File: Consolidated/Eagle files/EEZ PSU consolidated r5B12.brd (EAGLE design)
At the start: 337 x 150 mm, 555 parts, among them IC1 LTC3864EMSE#PBF, IC10 DAC8552IDGKTG4, IC11 ADG465SOT-23, IC12 TS5A9411DCKT, IC13 ADS1120IPWR, IC14 LP339D, IC15 TPD4E002DRLR, IC16 TPD2E001DZDR, IC17 ADUM3160BRWZ, IC18 TLC5925IDBQR, IC19 Si8641EC-B-IS1, IC2 LP2951SO8, IC20 SI8651EC-B-IS1, IC21 SI8651EC-B-IS1, IC22 LD1117ADT33TR, IC23 Si8641EC-B-IS1, IC24 PCA21125T/Q900/1,1, IC25 AT25256B-SSHL-B, IC26 W5500, IC27 BC857BS, IC28 TLC555, IC29 SN74LVC08APWR, IC3 TL783CKTTR, IC30 SN74LV1T34DBVR, IC31 TPS3705-33D, IC32 SN74LVC2G02DCTR, IC33 74LVC1G125GW.125, IC34 TPA6205A1DGN, IC4 LTC3260EMSE#PBF, IC5 TL072D, IC6 TL072D, IC7 LTC2050HVCS8#PBF, IC8 MCP23S17-E/SS, IC9 REF5025AIDG4, J1 BS-244DSM-R, J2 1-726388-2, J3 BS-244DSM-G, J4 BS-244DSM-B, J5 BS-244DSM-R, J6 BS-244DSM-B, J7 693072010801, Q1 IRFR5305, Q10 MMBT5401, Q11 MMBT5551, Q12 MMBT5551, Q13 IRLL2705PBF, Q14 IRFR48ZPBF, Q15 IRLML2246TRPBF, Q16 2N7002, Q17 MMBT5551, Q18 MMBT5401, Q19 MMBT5551, Q2 MMBT5401, Q20 MMBT5551, Q21 BTA26-600, Q22 BTA26-600, Q23 IRLL2705PBF, Q24 2N7002, Q25 2N7002, Q26 IRLML2246TRPBF, Q27 IRLML2246TRPBF, Q28 IRLML2246TRPBF, Q29 IRLML2246TRPBF, Q3 2N7002, Q30 2N7002, Q31 IRLML2246TRPBF, Q32 2N7002, Q33 2N7002, Q4 IRFP250N, Q5 BC857C, Q6 BCP56-16.115, Q7 IRFR5305, Q8 BCP56-16.115, Q9 MMBT5401, SW1 A101SYCQ04, SW2 EC12E20-24P24C-SW, SW3 1301.9316, X10 826629-5, X11 2411-01, X12 MC000006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

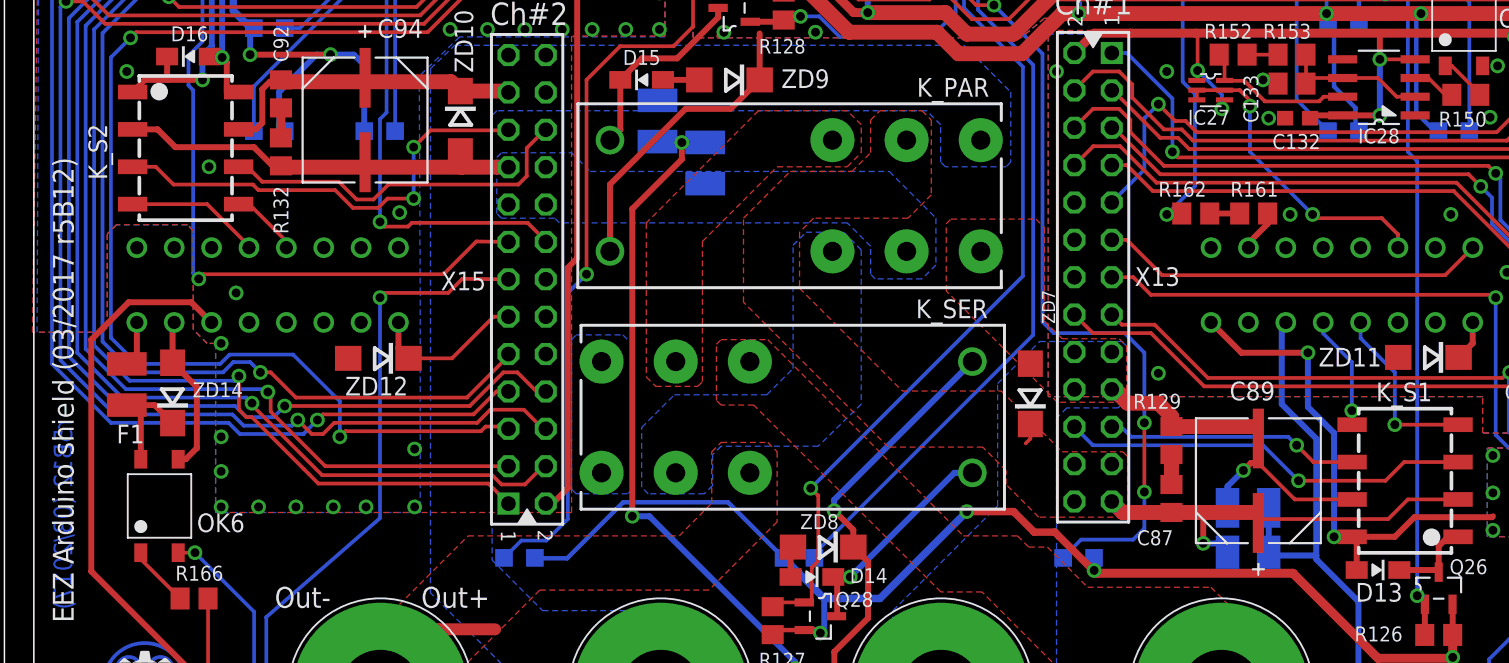
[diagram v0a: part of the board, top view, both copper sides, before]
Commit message: X14 pin 1, 2 swap, R177
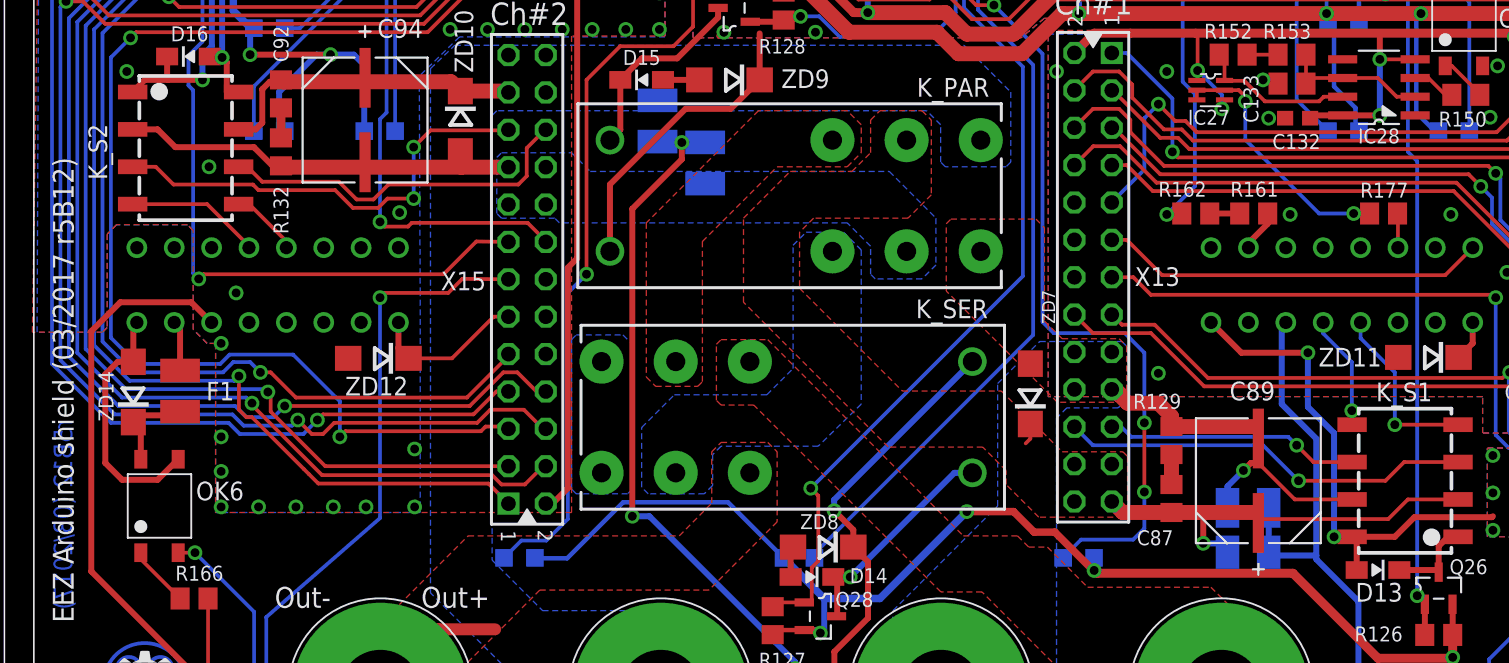
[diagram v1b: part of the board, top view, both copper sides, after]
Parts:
- added R177: 220R, rcl:R0805
- X1: value (none) -> 39-30-1039
- moved F1 3.65 mm to (118.9, 29.3)
- moved ZD14 2.67 mm to (115.8, 29.3)
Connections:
- removed net N$189: F1.2, X14.1, X14.1.1
- new net N$46: F1.2, X14.2, X14.2.1
- new net N$59: IC27.2, IC27.3, IC27.5, R177.2
- net N$188: now also X14.1, X14.1.1; no longer X14.2, X14.2.1
- net NTC_IN: now also R177.1; no longer IC27.2, IC27.3, IC27.5
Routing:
- net NTC_IN: track 21.3 -> 2.51 mm, vias 2 -> 0
- net N$59: track 0.00 -> 17.6 mm, vias 0 -> 2
- net N$188: track 10.9 -> 17.1 mm
- net N$46: track 0.00 -> 3.43 mm
- net N$189: track 3.10 -> 0.00 mm
- net N$187: track 7.43 -> 6.31 mm
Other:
- board text added: "R177"

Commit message: Encoder 25mm, new enclosure panels
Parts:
- SW2: value EC12E20-24P24C-SW -> PEC12R-4225F-S0024
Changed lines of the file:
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@@
 <attribute name="VALUE" x="102.0445" y="119.6975" size="1.27" layer="27" ratio="10"/>
 </element>
-<element name="SW2" library="EEZ_Lib1" package="EC12E_SW" value="EC12E20-24P24C-SW" x="216" y="62" smashed="yes" rot="MR270">
+<element name="SW2" library="EEZ_Lib1" package="EC12E_SW" value="PEC12R-4225F-S0024" x="216" y="62" smashed="yes" rot="MR270">
 <attribute name="NAME" x="209.185" y="69.7685" size="1.27" layer="26" rot="MR180"/>
 <attribute name="VALUE" x="206.455" y="62.5915" size="1.27" layer="28" rot="MR180"/>
@@
 </signal>
 </signals>
-<errors>
-</errors>
 </board>
 </drawing>

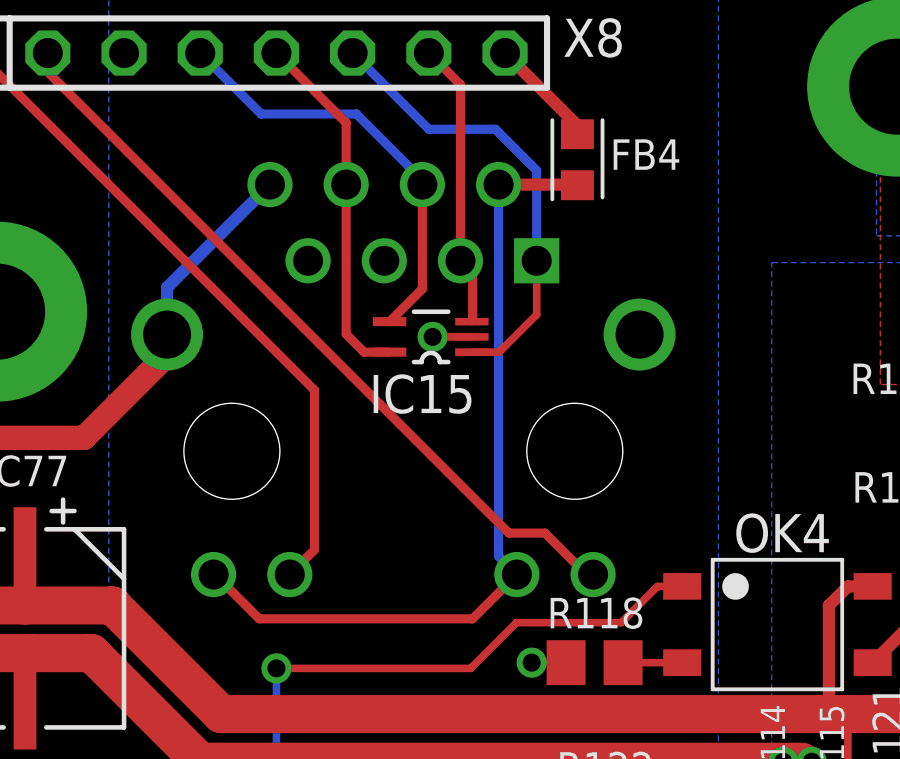
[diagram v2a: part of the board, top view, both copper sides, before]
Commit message: IC15 package, wire harness update
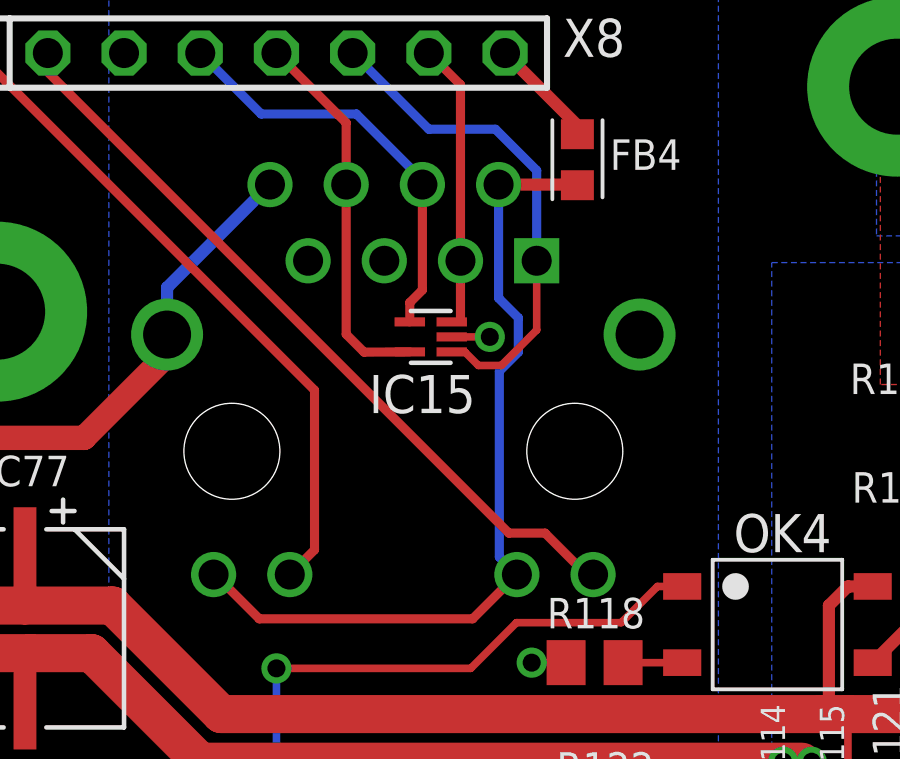
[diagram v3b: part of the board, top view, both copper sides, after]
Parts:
- IC15: value TPD4E002DRLR -> TPD4E002DRL; device EEZ_Lib1:SOT50P280X60-5N -> EEZ_Lib1:DRL5
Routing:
- net AUX_ETH_OUT+: track 15.2 -> 16.6 mm
- net AUX_ETH_IN-: track 12.0 -> 12.7 mm
- net N$24: track 27.2 -> 27.8 mm
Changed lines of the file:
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@@
 <layer number="17" name="Pads" color="6" fill="1" visible="yes" active="yes"/>
 <layer number="18" name="Vias" color="6" fill="1" visible="yes" active="yes"/>
-<layer number="19" name="Unrouted" color="14" fill="1" visible="no" active="yes"/>
+<layer number="19" name="Unrouted" color="14" fill="1" visible="yes" active="yes"/>
 <layer number="20" name="Dimension" color="15" fill="1" visible="yes" active="yes"/>
 <layer number="21" name="tPlace" color="7" fill="1" visible="yes" active="yes"/>
@@
 <attribute name="VALUE" x="91.948" y="47.8663" size="1.27" layer="27" ratio="10" rot="SR0"/>
 </element>
-<element name="IC15" library="EEZ_Lib1" package="SOT50P280X60-5N" value="TPD4E002DRLR" x="72.4535" y="61.6585" smashed="yes" rot="R180">
+<element name="IC15" library="EEZ_Lib1" package="DRL5" value="TPD4E002DRL" x="72.4535" y="61.6585" smashed="yes" rot="R180">
 <attribute name="NAME" x="70.3961" y="59.1185" size="1.27" layer="25" ratio="10" rot="SR0"/>
 <attribute name="VALUE" x="66.7766" y="61.1505" size="1.016" layer="27" ratio="10" rot="SR0"/>
@@
 <wire x1="79.6925" y1="110.744" x2="83.439" y2="110.744" width="1.016" layer="1"/>
 <wire x1="83.439" y1="110.744" x2="85.6615" y2="110.744" width="1.016" layer="1"/>
-<via x="72.517" y="61.6585" extent="1-16" drill="0.6" shape="octagon"/>
+<via x="74.422" y="61.6585" extent="1-16" drill="0.6" shape="octagon"/>
 <contactref element="IC29" pad="7"/>
 <contactref element="C134" pad="1"/>
@@
 <via x="99.314" y="117.602" extent="1-16" drill="0.6" shape="octagon"/>
 <wire x1="106.172" y1="133.604" x2="106.172" y2="134.112" width="0.254" layer="1"/>
-<wire x1="72.517" y1="61.6585" x2="73.8251" y2="61.6585" width="0.254" layer="1"/>
+<wire x1="74.422" y1="61.6585" x2="73.152" y2="61.6585" width="0.254" layer="1"/>
 <contactref element="J7" pad="6"/>
 <via x="268.4145" y="34.417" extent="1-16" drill="0.6" shape="octagon"/>
@@
 <wire x1="129.9845" y1="72.517" x2="116.2685" y2="82.2325" width="0" layer="19" extent="16-16"/>
 <wire x1="189" y1="39.08" x2="189" y2="34" width="0" layer="19" extent="1-1"/>
-<wire x1="73.8251" y1="61.6585" x2="83.566" y2="84.5845" width="0" layer="19" extent="1-1"/>
+<wire x1="74.422" y1="61.6585" x2="83.566" y2="84.5845" width="0" layer="19" extent="1-1"/>
 </signal>
 <signal name="+5V">
@@
 <contactref element="X8" pad="7"/>
 <contactref element="IC15" pad="3"/>
-<wire x1="73.8251" y1="62.1665" x2="73.8251" y2="62.2681" width="0.254" layer="1"/>
-<wire x1="73.8251" y1="62.2681" x2="73.8505" y2="62.2935" width="0.254" layer="1"/>
-<wire x1="73.8505" y1="62.2935" x2="73.8505" y2="63.7905" width="0.3048" layer="1"/>
-<wire x1="73.8505" y1="63.7905" x2="73.445" y2="64.196" width="0.3048" layer="1"/>
 <wire x1="73.445" y1="64.196" x2="73.445" y2="70.065" width="0.3048" layer="1"/>
 <wire x1="73.445" y1="70.065" x2="72.39" y2="71.12" width="0.3048" layer="1"/>
+<wire x1="73.445" y1="64.196" x2="73.445" y2="62.191" width="0.3048" layer="1"/>
+<wire x1="73.152" y1="62.1585" x2="73.4125" y2="62.1585" width="0.254" layer="1"/>
+<wire x1="73.4125" y1="62.1585" x2="73.445" y2="62.191" width="0.254" layer="1"/>
 </signal>
 <signal name="AUX_+3V3">
@@
 <contactref element="X8" pad="6"/>
 <contactref element="IC15" pad="1"/>
-<wire x1="75.985" y1="64.196" x2="75.985" y2="62.396" width="0.254" layer="1"/>
-<wire x1="75.985" y1="62.396" x2="74.7395" y2="61.1505" width="0.254" layer="1"/>
-<wire x1="73.8251" y1="61.1505" x2="74.7395" y2="61.1505" width="0.254" layer="1"/>
+<wire x1="75.985" y1="64.196" x2="75.985" y2="61.888" width="0.254" layer="1"/>
 <wire x1="75.985" y1="64.196" x2="75.985" y2="67.2075" width="0.3048" layer="16"/>
 <wire x1="75.985" y1="67.2075" x2="74.6125" y2="68.58" width="0.3048" layer="16"/>
 <wire x1="74.6125" y1="68.58" x2="72.39" y2="68.58" width="0.3048" layer="16"/>
 <wire x1="72.39" y1="68.58" x2="69.85" y2="71.12" width="0.3048" layer="16"/>
+<wire x1="75.985" y1="61.888" x2="74.803" y2="60.706" width="0.254" layer="1"/>
+<wire x1="74.803" y1="60.706" x2="74.041" y2="60.706" width="0.254" layer="1"/>
+<wire x1="74.041" y1="60.706" x2="73.5965" y2="61.1505" width="0.254" layer="1"/>
+<wire x1="73.5965" y1="61.1505" x2="73.16" y2="61.1505" width="0.254" layer="1"/>
+<wire x1="73.16" y1="61.1505" x2="73.152" y2="61.1585" width="0.254" layer="1"/>
 </signal>
 <signal name="AUX_ETH_IN-">
@@
 <wire x1="69.635" y1="66.736" x2="69.635" y2="61.7465" width="0.3048" layer="1"/>
 <wire x1="69.635" y1="61.7465" x2="70.231" y2="61.1505" width="0.3048" layer="1"/>
-<wire x1="70.231" y1="61.1505" x2="71.0819" y2="61.1505" width="0.3048" layer="1"/>
+<wire x1="70.231" y1="61.1505" x2="71.755" y2="61.1585" width="0.3048" layer="1"/>
 <wire x1="69.635" y1="66.736" x2="69.635" y2="68.795" width="0.3048" layer="1"/>
 <wire x1="69.635" y1="68.795" x2="67.31" y2="71.12" width="0.3048" layer="1"/>
@@
 <contactref element="X8" pad="4"/>
 <contactref element="IC15" pad="4"/>
-<wire x1="72.175" y1="66.736" x2="72.175" y2="63.2596" width="0.3048" layer="1"/>
-<wire x1="72.175" y1="63.2596" x2="71.0819" y2="62.1665" width="0.3048" layer="1"/>
+<wire x1="72.175" y1="66.736" x2="72.175" y2="63.2215" width="0.3048" layer="1"/>
 <wire x1="72.175" y1="66.736" x2="72.175" y2="66.89" width="0.3048" layer="16"/>
 <wire x1="72.175" y1="66.89" x2="69.977" y2="69.088" width="0.3048" layer="16"/>
 <wire x1="69.977" y1="69.088" x2="66.802" y2="69.088" width="0.3048" layer="16"/>
 <wire x1="66.802" y1="69.088" x2="64.77" y2="71.12" width="0.3048" layer="16"/>
+<wire x1="72.175" y1="63.2215" x2="71.755" y2="62.8015" width="0.3048" layer="1"/>
+<wire x1="71.755" y1="62.8015" x2="71.755" y2="62.1585" width="0.3048" layer="1"/>
 </signal>
 <signal name="AUX_ETH_ACTLED">
@@
 <wire x1="74.715" y1="66.736" x2="77.343" y2="66.736" width="0.4064" layer="1"/>
 <wire x1="77.343" y1="66.736" x2="77.343" y2="66.714" width="0.4064" layer="1"/>
-<wire x1="74.715" y1="66.736" x2="74.715" y2="54.346" width="0.3048" layer="16"/>
-<wire x1="74.715" y1="54.346" x2="75.325" y2="53.736" width="0.3048" layer="16"/>
+<wire x1="74.715" y1="66.736" x2="74.715" y2="62.953" width="0.3048" layer="16"/>
+<wire x1="74.715" y1="62.953" x2="75.3745" y2="62.2935" width="0.3048" layer="16"/>
+<wire x1="75.3745" y1="62.2935" x2="75.3745" y2="61.1505" width="0.3048" layer="16"/>
+<wire x1="75.3745" y1="61.1505" x2="74.7395" y2="60.5155" width="0.3048" layer="16"/>
+<wire x1="74.7395" y1="60.5155" x2="74.7395" y2="54.3215" width="0.3048" layer="16"/>
+<wire x1="74.7395" y1="54.3215" x2="75.325" y2="53.736" width="0.3048" layer="16"/>
 </signal>
 <signal name="EXTSD_CS">
@@
 </signal>
 </signals>
+<errors>
+</errors>
 </board>
 </drawing>

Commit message: #32 (R64 changed to 10K)
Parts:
- R64: value 2K2 -> 10K
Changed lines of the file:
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@@
 <layer number="25" name="tNames" color="7" fill="1" visible="yes" active="yes"/>
 <layer number="26" name="bNames" color="13" fill="1" visible="no" active="yes"/>
-<layer number="27" name="tValues" color="10" fill="1" visible="no" active="yes"/>
+<layer number="27" name="tValues" color="10" fill="1" visible="yes" active="yes"/>
 <layer number="28" name="bValues" color="11" fill="1" visible="no" active="yes"/>
 <layer number="29" name="tStop" color="7" fill="9" visible="no" active="yes"/>
@@
 <layer number="37" name="tTest" color="7" fill="1" visible="no" active="yes"/>
 <layer number="38" name="bTest" color="7" fill="1" visible="no" active="yes"/>
-<layer number="39" name="tKeepout" color="15" fill="1" visible="no" active="yes"/>
+<layer number="39" name="tKeepout" color="15" fill="1" visible="yes" active="yes"/>
 <layer number="40" name="bKeepout" color="13" fill="1" visible="no" active="yes"/>
 <layer number="41" name="tRestrict" color="4" fill="10" visible="no" active="yes"/>
@@
 <layer number="127" name="_tValues" color="7" fill="1" visible="no" active="no"/>
 <layer number="128" name="_bValues" color="7" fill="1" visible="no" active="no"/>
-<layer number="129" name="rear_panel" color="10" fill="1" visible="no" active="yes"/>
+<layer number="129" name="rear_panel" color="10" fill="1" visible="yes" active="yes"/>
 <layer number="131" name="tAdjust" color="7" fill="1" visible="no" active="no"/>
 <layer number="132" name="bAdjust" color="7" fill="1" visible="no" active="no"/>
@@
 <attribute name="VALUE" x="26.035" y="108.6485" size="1.016" layer="27" ratio="10" rot="R180"/>
 </element>
-<element name="R64" library="rcl" package="R0805" value="2K2" x="43.1061" y="104.4608" smashed="yes" rot="R180">
+<element name="R64" library="rcl" package="R0805" value="10K" x="43.1061" y="104.4608" smashed="yes" rot="R180">
 <attribute name="NAME" x="41.9839" y="105.5337" size="0.9906" layer="25" ratio="10"/>
 <attribute name="VALUE" x="41.5867" y="103.9594" size="1.016" layer="27" ratio="10"/>
@@
 <element name="IC7" library="EEZ_Lib1" package="SOIC127P600X173-8N" value="LTC2050HVCS8#PBF" x="45.0215" y="100.6475" smashed="yes" rot="R180">
 <attribute name="NAME" x="47.1551" y="96.3295" size="1.27" layer="25" ratio="10" rot="SR0"/>
-<attribute name="VALUE" x="41.7036" y="100.249" size="1.016" layer="27" ratio="10" rot="SR0"/>
+<attribute name="VALUE" x="41.0686" y="99.106" size="0.8128" layer="27" ratio="10" rot="SR0"/>
 </element>
 <element name="C46" library="rcl" package="C0805" value="1u" x="38.9255" y="104.013" smashed="yes">
@@
 </signal>
 </signals>
-<errors>
-</errors>
 </board>
 </drawing>

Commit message: #33, #34
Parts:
- removed X21: ZL262-5SG, con-samtec:SSW-105-02-S-S
- R63: value 0R2 -> 0R16
- R65: value 0R020 -> 0R020 (1-3W)
- X7: value LMJ2138814S0L1T1C -> Amphenol: LMJ2138812S0LOT6C or WE: 74990101210
- moved X8 5.08 mm to (71.1, 71.1)
- moved IC15 1.65 mm to (74.1, 61.7)
- moved FB4 1.06 mm to (78.4, 67.9), turned to 0 degrees
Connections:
- net AUX_ETH_ACTLED: now also X7.10; no longer X7.9
- net AUX_ETH_IN+: now also X7.3; no longer X7.4
- net AUX_ETH_LINKLED: now also X7.12; no longer X7.11
- net AUX_ETH_OUT+: now also X7.2; no longer X7.1
- net AUX_ETH_OUT-: now also X7.1; no longer X7.3
- net DC_OUT: no longer X21.5
- net FB: no longer X21.4
- net N$24: now also X7.11, X7.4, X7.9; no longer X7.10, X7.12, X7.2
- net OUT+: no longer X21.3
- net PREG_OUT: no longer X21.2
- net V-: no longer X21.1
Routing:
- net PREG_OUT: track 21.6 -> 5.24 mm, vias 2 -> 0
- net FB: track 32.7 -> 16.6 mm
- net OUT+: track 243.7 -> 235.2 mm
- net V-: track 144.8 -> 137.9 mm, vias 12 -> 11
- net N$24: track 27.8 -> 34.2 mm
- net DC_OUT: track 140.0 -> 134.2 mm
- net AUX_ETH_OUT+: track 16.6 -> 11.8 mm, vias 0 -> 1
- net AUX_ETH_ACTLED: track 25.7 -> 21.8 mm
- net AUX_ETH_IN+: track 14.1 -> 10.8 mm
- net +5V: track 970.0 -> 968.8 mm
- net AUX_ETH_IN-: track 12.7 -> 13.8 mm
- net AUX_ETH_LINKLED: track 22.6 -> 21.7 mm
- net AUX_ETH_OUT-: track 9.67 -> 10.2 mm
- net GND: vias 416 -> 417
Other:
- board text added: "EEZ AUX PS r5B12a"
- board text added: "EEZ AUX PS r5B12a (03/2017)"
- board text removed: "EEZ AUX PS r5B12"
- board text removed: "EEZ AUX PS r5B12 (03/2017)"
- board text removed: "X21"

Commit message: #38
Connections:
- net DC+: now also L1.3; no longer L1.2
- net DC_OUT: now also L1.4; no longer L1.3
- net GND: now also L1.2; no longer L1.4
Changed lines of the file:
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@@
 <via x="265.5062" y="10.033" extent="1-16" drill="0.6" shape="octagon"/>
 <via x="116.6495" y="138.811" extent="1-16" drill="0.6" shape="octagon"/>
-<contactref element="L1" pad="4"/>
+<contactref element="L1" pad="2"/>
 <via x="101.854" y="117.602" extent="1-16" drill="0.6" shape="octagon"/>
 <via x="104.394" y="117.602" extent="1-16" drill="0.6" shape="octagon"/>
@@
 <wire x1="119.873" y1="129.159" x2="119.873" y2="131.7094" width="0.6096" layer="1"/>
 <wire x1="119.873" y1="131.7094" x2="119.9261" y2="131.7625" width="0.6096" layer="1"/>
-<contactref element="L1" pad="3"/>
+<contactref element="L1" pad="4"/>
 <wire x1="112.014" y1="112.0775" x2="112.014" y2="105.664" width="0.254" layer="16"/>
 <via x="112.014" y="105.664" extent="1-16" drill="0.6" shape="octagon"/>
@@
 <signal name="DC+">
 <contactref element="C1" pad="2"/>
-<contactref element="L1" pad="2"/>
+<contactref element="L1" pad="3"/>
 <polygon width="0.254" layer="1" isolate="0.3048" thermals="no">
 <vertex x="155.2575" y="97.155"/>

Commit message: #39 eagle files
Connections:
- net N$157 renamed EOUT_B
- net N$159 renamed EOUT_A
- net ENC_A: now also C138.1, MCU.A9, R165.1; no longer C137.2, MCU.A8, R157.1
- net ENC_B: now also C137.2, MCU.A8, R157.1; no longer C138.1, MCU.A9, R165.1
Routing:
- net ENC_B: track 8.23 -> 7.36 mm
- net ENC_A: track 7.36 -> 8.23 mm
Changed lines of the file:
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@@
 <wire x1="130.49" y1="110.871" x2="130.49" y2="111.186" width="0.8128" layer="1"/>
 </signal>
-<signal name="N$157">
+<signal name="EOUT_B">
 <contactref element="R157" pad="2"/>
 <contactref element="R156" pad="2"/>
@@
 <wire x1="246.38" y1="57.8485" x2="245.9355" y2="57.404" width="0.254" layer="1"/>
 </signal>
-<signal name="ENC_A">
+<signal name="ENC_B">
 <contactref element="C137" pad="2"/>
 <contactref element="R157" pad="1"/>
@@
 <wire x1="264.2235" y1="23.522" x2="264.6062" y2="23.152" width="0.254" layer="16"/>
 </signal>
-<signal name="ENC_B">
+<signal name="ENC_A">
 <contactref element="R165" pad="1"/>
 <contactref element="C138" pad="1"/>
@@
 <wire x1="262.0662" y1="26.3" x2="260.6802" y2="27.686" width="0.254" layer="16"/>
 </signal>
-<signal name="N$159">
+<signal name="EOUT_A">
 <contactref element="R165" pad="2"/>
 <contactref element="R159" pad="2"/>
